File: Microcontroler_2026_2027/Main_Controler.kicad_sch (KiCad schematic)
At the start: 48 parts, among them J1 Conn_01x03, J2 Screw_Terminal_01x04, J4 Brake Light, J6 TC2030, Q2 AO3401A, U1 STM32H750VBTx, U10 TLV75533PDBV, U2 SN65HVD230, U3 SFH617A-1, U8 LMR33630ADDA

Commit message: Branch initial commit / TC2030 wired
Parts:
- removed J6: TC2030, Connector:Tag-Connect_TC2030-IDC-NL_2x03_P1.27mm_Vertical, symbol Connector:TC2030
- added C44: 4.7uF, Capacitor_SMD:C_1206_3216Metric, symbol Device:C_Small
- added C45: 100nF, Capacitor_SMD:C_1206_3216Metric, symbol Device:C_Small
- added C46, C47: 10pF, Capacitor_SMD:C_1206_3216Metric, symbol Device:C_Small
- added J6: ST-LINK TC2030, Connector:Tag-Connect_TC2030-IDC-FP_2x03_P1.27mm_Vertical, symbol Connector:Conn_ARM_SWD_TagConnect_TC2030
- added R3: 10, Package_DFN_QFN:QFN-56-1EP_7x7mm_P0.4mm_EP5.6x5.6mm, symbol Device:R_Small
- added U4: SX1280IMLTRT, QFN50P400X400X100-25N-D, symbol SX1280IMLTRT:SX1280IMLTRT
- added Y1: 52Mhz, QFN50P400X400X100-25N-D, symbol Device:Crystal_GND23_Small
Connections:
- net +3.3V: now also C44.2
- net GND: now also C44.1, C45.1, C46.1, C47.1, J6.5 (GND), U4.13 (GND_2), U4.20 (GND_3), U4.21 (GND_4), U4.23 (GND_5), U4.24 (GND_6), U4.5 (GND_1), Y1.2 (G), Y1.3 (G)
- net SWCLK: now also J6.4 (SWCLK)
- net SWDIO: now also J6.2 (SWDIO)
- net VCC: now also C45.2, J6.1 (VCC), U4.11 (VBAT_IO), U4.15 (VBAT), U4.2 (VDD_IN)
- net NRST: now reaches C4.2, J1.2 (Pin_2), R1.2, U1.14 (NRST)
- net NRST: now also J6.3 (~{RESET})
- new net: C47.2, U4.6 (XTB), Y1.1
- new net: C46.2, R3.1, Y1.4
- new net: R3.2, U4.4 (XTA)
- new net SWO: J6.6 (SWO)
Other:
- note added: "2.4Ghz LoRa Transceiver"
- note removed: "A FINIR"

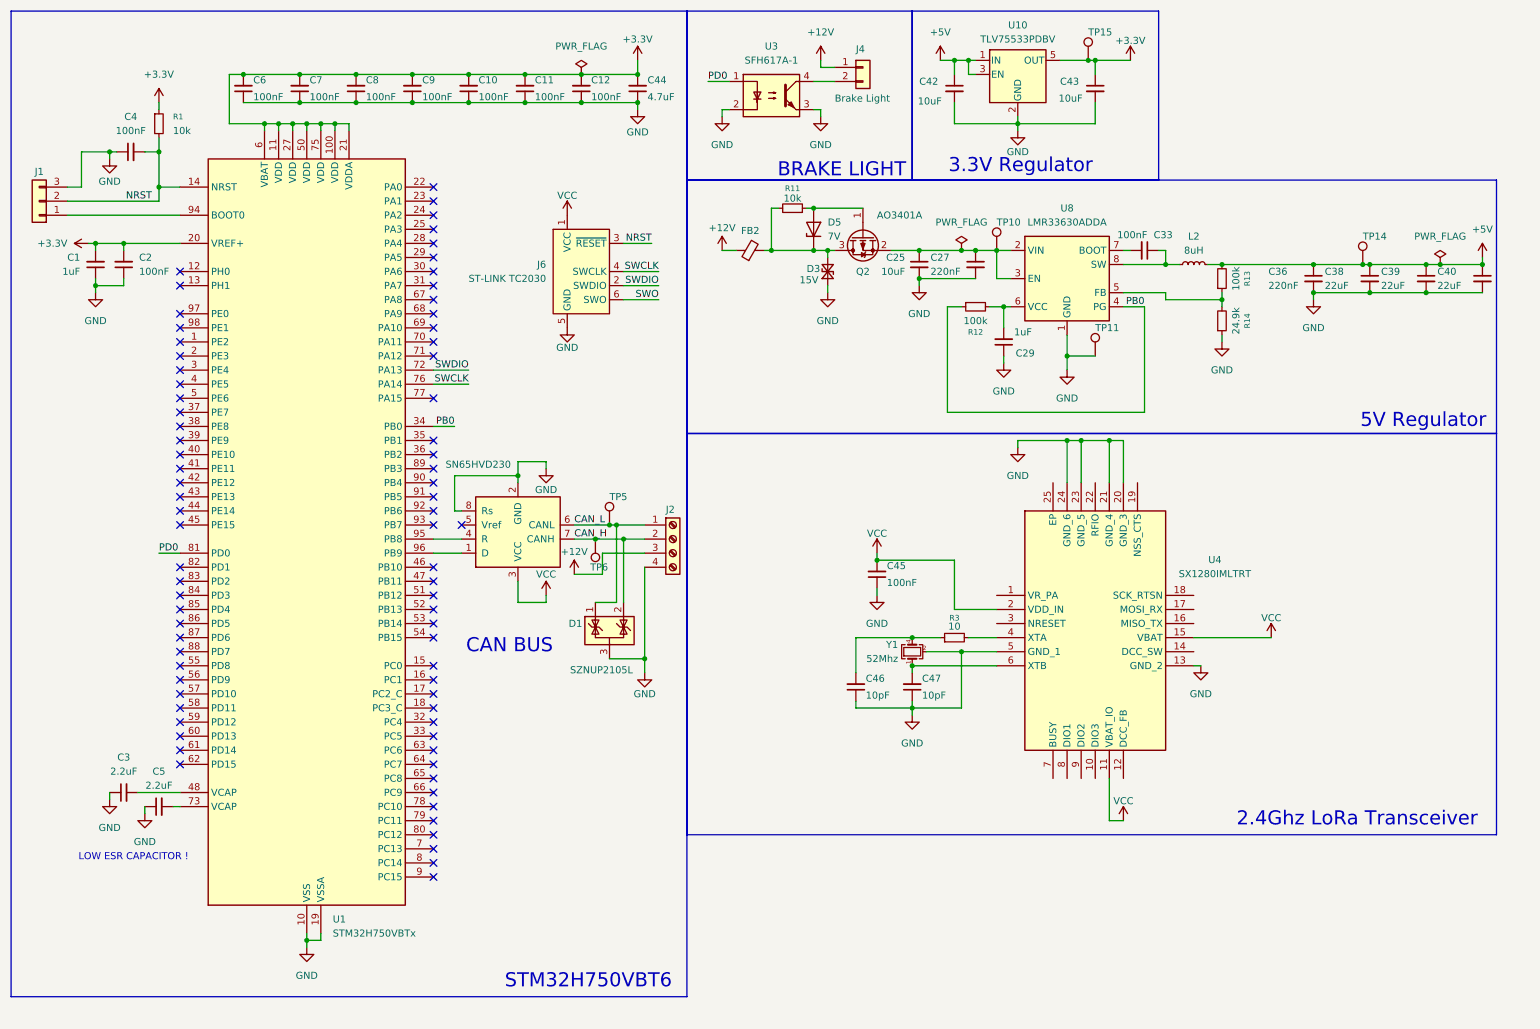
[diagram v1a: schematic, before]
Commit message: SX1280 Transceiver wired
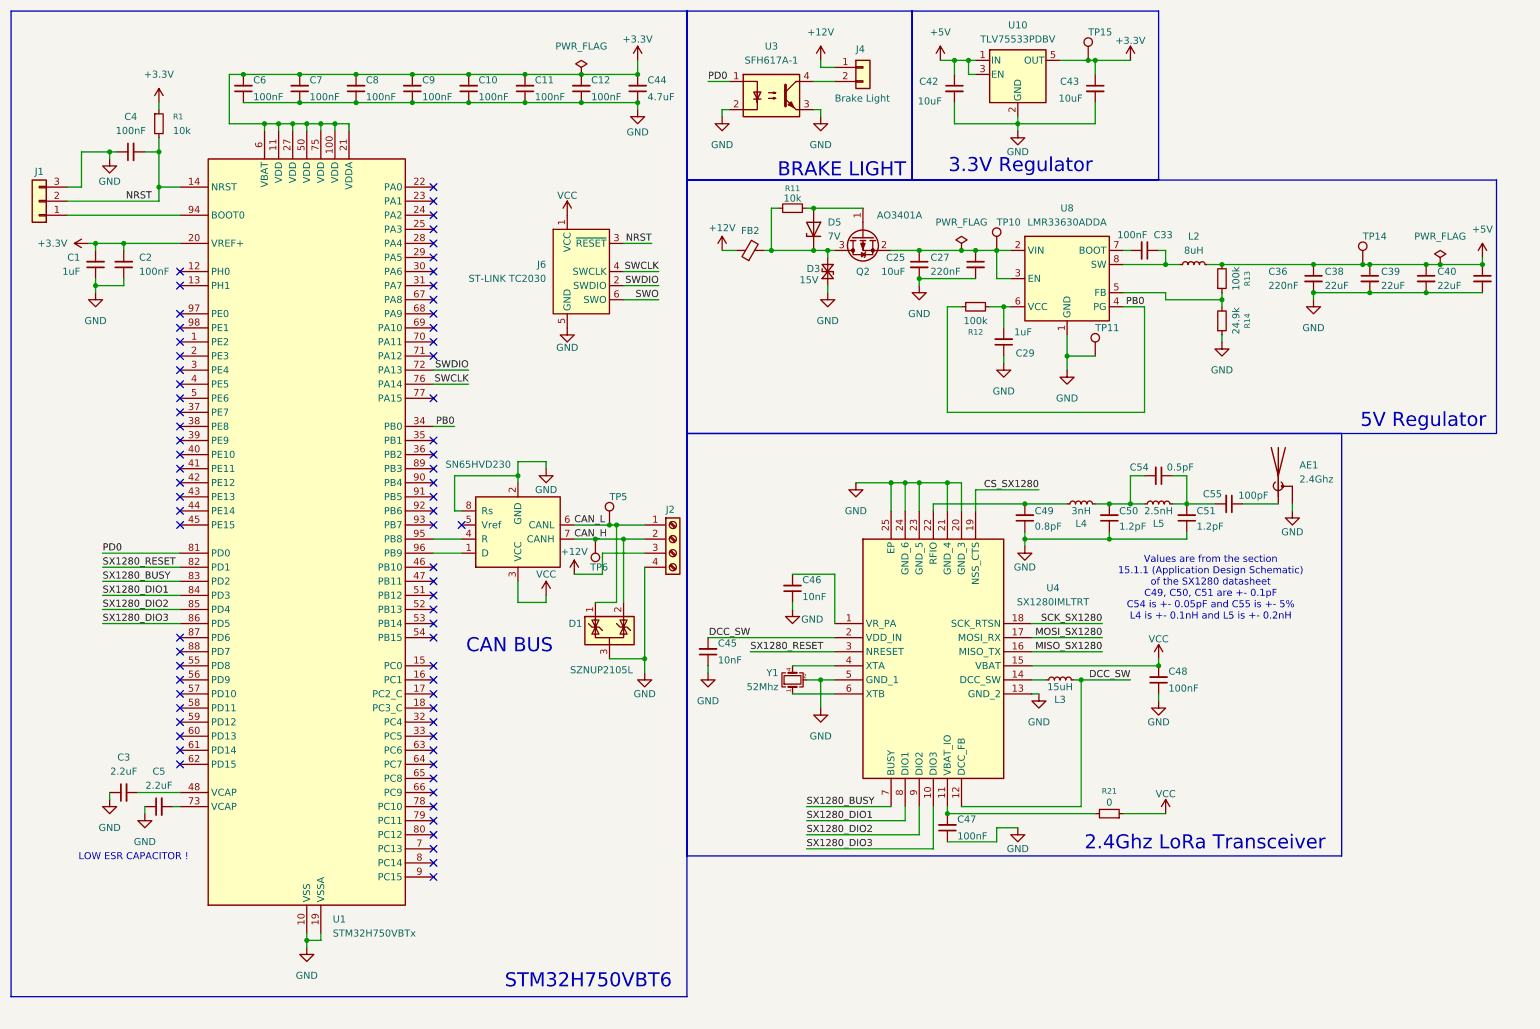
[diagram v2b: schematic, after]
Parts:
- removed R3: 10, Package_DFN_QFN:QFN-56-1EP_7x7mm_P0.4mm_EP5.6x5.6mm, symbol Device:R_Small
- added AE1: 2.4Ghz, symbol Device:Antenna_Shield
- added C48: 100nF, Capacitor_SMD:C_1206_3216Metric, symbol Device:C_Small
- added C49: 0.8pF, Capacitor_SMD:C_1206_3216Metric, symbol Device:C_Small
- added C50, C51: 1.2pF, Capacitor_SMD:C_1206_3216Metric, symbol Device:C_Small
- added C54: 0.5pF, Capacitor_SMD:C_1206_3216Metric, symbol Device:C_Small
- added C55: 100pF, Capacitor_SMD:C_1206_3216Metric, symbol Device:C_Small
- added L3: 15uH, symbol Device:L_Small
- added L4: 3nH, symbol Device:L_Small
- added L5: 2.5nH, symbol Device:L_Small
- added R21: 0, Resistor_SMD:R_1206_3216Metric, symbol Device:R_Small
- C45: value 100nF -> 10nF
- C46: value 10pF -> 10nF
- C47: value 10pF -> 100nF
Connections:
- net GND: now also U4.25 (EP), AE1.2 (Shield), C48.1, C49.1, C50.1, C51.1
- net VCC: now also C48.2, R21.1; no longer C45.2, U4.11 (VBAT_IO), U4.2 (VDD_IN)
- net at U4.6 (XTB), Y1.1: no longer C47.2
- net at Y1.4: now also U4.4 (XTA); no longer C46.2
- net SX1280_RESET: now reaches U1.82 (PD1)
- net SX1280_RESET: now also U4.3 (NRESET)
- net SX1280_BUSY: now reaches U1.83 (PD2)
- net SX1280_BUSY: now also U4.7 (BUSY)
- net SX1280_DIO1: now reaches U1.84 (PD3)
- net SX1280_DIO1: now also U4.8 (DIO1)
- net SX1280_DIO2: now reaches U1.85 (PD4)
- net SX1280_DIO2: now also U4.9 (DIO2)
- net SX1280_DIO3: now reaches U1.86 (PD5)
- net SX1280_DIO3: now also U4.10 (DIO3)
- net at U4.1 (VR_PA): now also C46.2
- net DCC_SW: now reaches U4.12 (DCC_FB)
- net DCC_SW: now also C45.2, U4.2 (VDD_IN), L3.2
- net at U4.14 (DCC_SW): now also L3.1
- net MISO_SX1280: now reaches U4.16 (MISO_TX)
- net MOSI_SX1280: now reaches U4.17 (MOSI_RX)
- net SCK_SX1280: now reaches U4.18 (SCK_RTSN)
- net CS_SX1280: now reaches U4.19 (NSS_CTS)
- net at U4.22 (RFIO): now also C49.2, L4.1
- new net: AE1.1 (A), C55.1
- new net: C51.2, C54.1, C55.2, L5.2
- new net: C50.2, C54.2, L4.2, L5.1
- new net: C47.2, R21.2, U4.11 (VBAT_IO)
- no-connect marks 77 -> 72
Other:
- note added: "Values are from the section 15.1.1 (Application Design Schematic) of the SX1280 datasheet C49, C50, C51 are +- 0.1pF C54 is +- 0.05pF and C55 is +- 5% L4 is +- 0.1nH and L5 is +- 0.2nH"
- moved on the sheet: C45, U4, Y1

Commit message: Added telemetry station schematic and wired SPI to the main controller
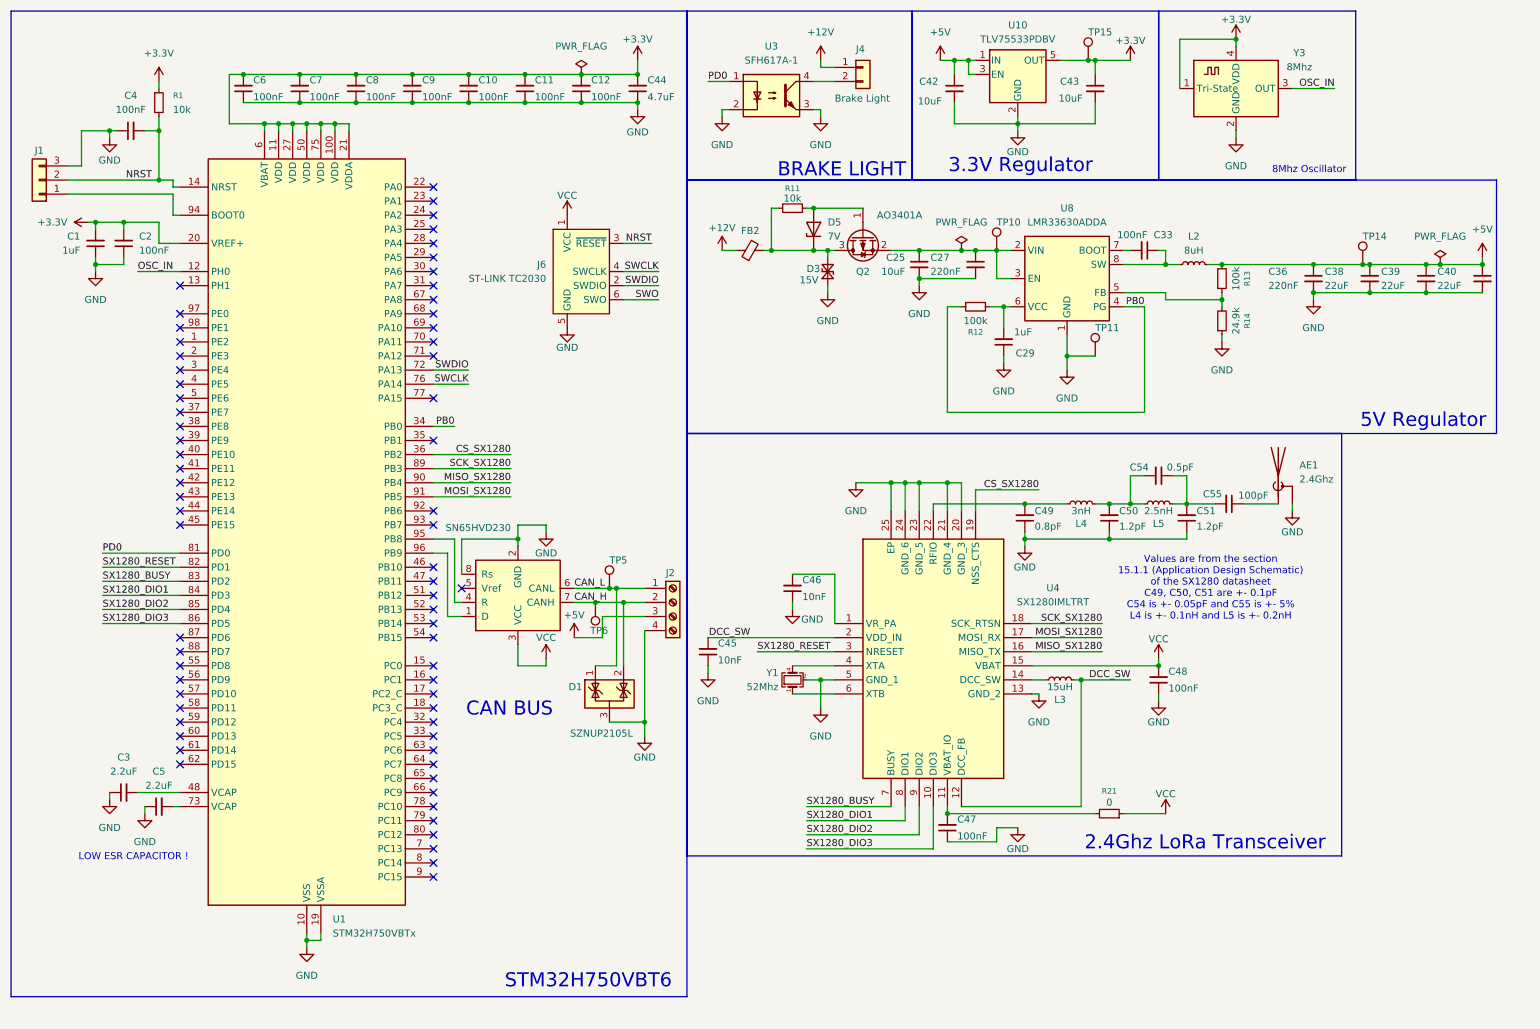
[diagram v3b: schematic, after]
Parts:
- added Y3: 8Mhz, Oscillator:Oscillator_SMD_Abracon_ASCO-4Pin_1.6x1.2mm, symbol Oscillator:ASCO
- U4: footprint QFN50P400X400X100-25N-D -> sx1280imltrt:QFN50P400X400X100-25N-D
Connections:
- net +12V: no longer J2.3 (Pin_3)
- net +3.3V: now also Y3.1 (Tri-State), Y3.4 (VDD)
- net +5V: now also J2.3 (Pin_3)
- net CS_SX1280: now also U1.36 (PB2)
- net GND: now also Y3.2 (GND)
- net MISO_SX1280: now also U1.90 (PB4)
- net MOSI_SX1280: now also U1.91 (PB5)
- net SCK_SX1280: now also U1.89 (PB3)
- net OSC_IN: now reaches U1.12 (PH0)
- net OSC_IN: now also Y3.3 (OUT)
- no-connect marks 72 -> 67
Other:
- note added: "8Mhz Oscillator"
- moved on the sheet: C1, C2, C4, D1, J1, J2, R1, TP5, TP6

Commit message: updated components footprints
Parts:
- removed AE1: 2.4Ghz, symbol Device:Antenna_Shield
- removed C49: 0.8pF, Capacitor_SMD:C_1206_3216Metric, symbol Device:C_Small
- removed C50, C51: 1.2pF, Capacitor_SMD:C_1206_3216Metric, symbol Device:C_Small
- removed C54: 0.5pF, Capacitor_SMD:C_1206_3216Metric, symbol Device:C_Small
- removed C55: 100pF, Capacitor_SMD:C_1206_3216Metric, symbol Device:C_Small
- removed L4: 3nH, symbol Device:L_Small
- removed L5: 2.5nH, symbol Device:L_Small
- added C21: 0.8pF, Capacitor_SMD:C_0402_1005Metric, symbol Device:C_Small
- added C23, C27: 1.2pF, Capacitor_SMD:C_0402_1005Metric, symbol Device:C_Small
- added C25: 0.5pF, Capacitor_SMD:C_0402_1005Metric, symbol Device:C_Small
- added C28: 100pF, Capacitor_SMD:C_0402_1005Metric, symbol Device:C_Small
- added J5: 2.4Ghz, Connector_Coaxial:SMA_Amphenol_132134_Vertical, symbol Connector:Conn_Coaxial_Small
- added L2: 3nH, Inductor_SMD:L_0402_1005Metric, symbol Device:L_Small
- added L3: 2.5nH, Inductor_SMD:L_0402_1005Metric, symbol Device:L_Small
- renumbered C44 to C13, C45 to C14, C46 to C15, C25 to C16, C47 to C17, C42 to C18, C27 to C19, C29 to C20, C43 to C22, C33 to C24, C48 to C26, C36 to C29, C38 to C30, C39 to C31, C40 to C32, D5 to D2, FB2 to FB1, J6 to J2, J2 to J3, L3 to L1, L2 to L4, Q2 to Q1, R11 to R2, R12 to R3, R21 to R4, R13 to R5, R14 to R6, TP6 to TP1, TP5 to TP2, TP10 to TP3, TP15 to TP4, TP11 to TP5, TP14 to TP6, U10 to U5, U8 to U6, Y3 to Y2
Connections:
- net GND: now also C21.1, C23.1, C27.1, J5.2 (Ext)
- net at U4.22 (RFIO): now also C21.2, L2.1
- new net: C23.2, C25.2, L2.2, L3.1
- new net: C25.1, C27.2, C28.2, L3.2
- new net: C28.1, J5.1 (In)
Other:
- note added: "Values are from the section 15.1.1 (Application Design Schematic) of the SX1280 datasheet C21, C23, C27 are +- 0.1pF C25 is +- 0.05pF and C28 is +- 5% L2 is +- 0.1nH and L3 is +- 0.2nH"
- note removed: "Values are from the section 15.1.1 (Application Design Schematic) of the SX1280 datasheet C49, C50, C51 are +- 0.1pF C54 is +- 0.05pF and C55 is +- 5% L4 is +- 0.1nH and L5 is +- 0.2nH"
